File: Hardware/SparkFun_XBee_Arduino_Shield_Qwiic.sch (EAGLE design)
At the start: 68 parts, among them J4 QWIIC_RIGHT_ANGLE, U1 FSUSB30MUX_MSOP10, U2 AP63203, U3 ESD Diode, U4 FT231XS, U5 ESD Diode, U6 TXS0108, U7 TXS0108

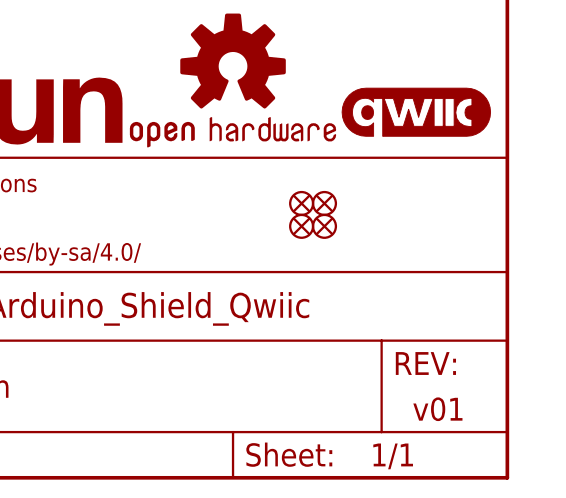
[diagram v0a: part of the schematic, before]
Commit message: Fixes wire stub DRC error
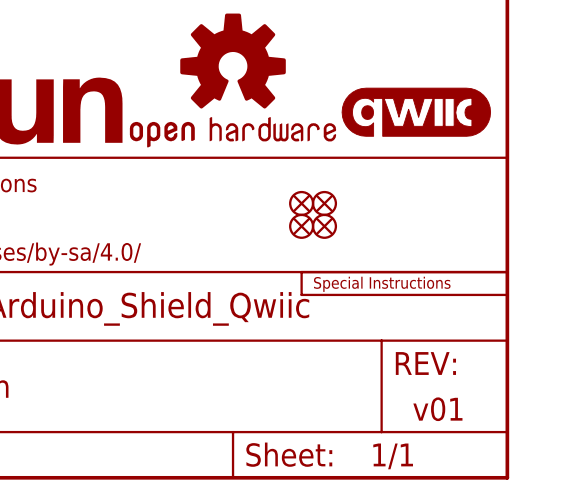
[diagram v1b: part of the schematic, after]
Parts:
- added LOGO4: SPECIAL_INSTRUCTIONS-ORDERING, SparkFun-Aesthetics:SPECIAL_INSTRUCTIONS-ORDERING
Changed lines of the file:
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@@
 <part name="SUPPLY27" library="SparkFun-PowerSymbols" deviceset="3.3V" device=""/>
 <part name="LOGO1" library="SparkFun-Aesthetics" deviceset="SFE_LOGO_NAME" device="BLANK"/>
+<part name="LOGO4" library="SparkFun-Aesthetics" deviceset="SPECIAL_INSTRUCTIONS" device="-ORDERING"/>
 </parts>
 <sheets>
@@
 </instance>
 <instance part="LOGO1" gate="G$1" x="332.74" y="33.02" smashed="yes"/>
+<instance part="LOGO4" gate="G$1" x="408.94" y="20.32" smashed="yes"/>
 </instances>
 <busses>

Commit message: Rolls to v02
* Fixes USB data lines on main UART
* Shifts ASC, RSSI nets to LEDs to be non-translated by default
* Move SCL data line to non-translated by default
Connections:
- net D+: now also U4.USBDP; no longer U4.USBDM
- net D-: now also U4.USBDM; no longer U4.USBDP
- net D1/SCL: now also J4.4, R15.1
- net D1/SCL-TRANS: no longer J4.4, R15.1
- net D10/RSSI_PWM: now also R2.1
- net D10/RSSI_PWM-TRANS: no longer R2.1
- net D5/ASSOCIATE: now also R12.1
- net D5/ASSOCIATE-TRANS: no longer R12.1
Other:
- note added: "v02"
- note removed: "v01"
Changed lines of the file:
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@@
 <text x="223.774" y="271.526" size="2.54" layer="94" font="vector" align="center">Buck Converter - AP63203</text>
 <text x="388.62" y="93.98" size="2.54" layer="94" font="vector" align="center">Qwiic - I2C</text>
-<text x="424.18" y="7.62" size="2.54" layer="94" font="vector" align="center">v01</text>
+<text x="424.18" y="7.62" size="2.54" layer="94" font="vector" align="center">v02</text>
 <text x="363.22" y="10.16" size="2.54" layer="94" font="vector" align="center">Elias Santistevan</text>
 <text x="187.96" y="71.12" size="2.54" layer="94" font="vector" align="center">Buttons and LEDs</text>
@@
 <pinref part="U6" gate="G$1" pin="A1"/>
 </segment>
+<segment>
+<pinref part="R15" gate="G$1" pin="1"/>
+<wire x1="360.68" y1="58.42" x2="363.22" y2="58.42" width="0.1524" layer="91"/>
+<label x="360.68" y="58.42" size="1.27" layer="95" font="vector" rot="R180" xref="yes"/>
+</segment>
+<segment>
+<pinref part="J4" gate="G$1" pin="4"/>
+<wire x1="406.4" y1="71.12" x2="411.48" y2="71.12" width="0.1524" layer="91"/>
+<label x="411.48" y="71.12" size="1.27" layer="95" font="vector" xref="yes"/>
+</segment>
 </net>
 <net name="GND" class="0">
@@
 <pinref part="U7" gate="G$1" pin="A2"/>
 </segment>
+<segment>
+<pinref part="R2" gate="G$1" pin="1"/>
+<label x="175.26" y="48.26" size="1.27" layer="95" font="vector" xref="yes"/>
+<wire x1="172.72" y1="45.72" x2="172.72" y2="48.26" width="0.1524" layer="91"/>
+<wire x1="172.72" y1="48.26" x2="175.26" y2="48.26" width="0.1524" layer="91"/>
+</segment>
 </net>
 <net name="D8/!DTR!" class="0">
@@
 <label x="365.76" y="132.08" size="1.27" layer="95" font="vector" rot="R180" xref="yes"/>
 <pinref part="U7" gate="G$1" pin="A4"/>
+</segment>
+<segment>
+<pinref part="R12" gate="G$1" pin="1"/>
+<label x="175.26" y="50.8" size="1.27" layer="95" font="vector" xref="yes"/>
+<wire x1="167.64" y1="45.72" x2="167.64" y2="50.8" width="0.1524" layer="91"/>
+<wire x1="167.64" y1="50.8" x2="175.26" y2="50.8" width="0.1524" layer="91"/>
 </segment>
 </net>
@@
 </segment>
 <segment>
-<label x="25.4" y="114.3" size="1.27" layer="95" font="vector" rot="R180" xref="yes"/>
-<pinref part="U4" gate="U$1" pin="USBDM"/>
-<wire x1="25.4" y1="114.3" x2="30.48" y2="114.3" width="0.1524" layer="91"/>
+<label x="25.4" y="111.76" size="1.27" layer="95" font="vector" rot="R180" xref="yes"/>
+<pinref part="U4" gate="U$1" pin="USBDP"/>
+<wire x1="25.4" y1="111.76" x2="30.48" y2="111.76" width="0.1524" layer="91"/>
 </segment>
 </net>
@@
 </segment>
 <segment>
-<label x="25.4" y="111.76" size="1.27" layer="95" font="vector" rot="R180" xref="yes"/>
-<pinref part="U4" gate="U$1" pin="USBDP"/>
-<wire x1="25.4" y1="111.76" x2="30.48" y2="111.76" width="0.1524" layer="91"/>
+<label x="25.4" y="114.3" size="1.27" layer="95" font="vector" rot="R180" xref="yes"/>
+<pinref part="U4" gate="U$1" pin="USBDM"/>
+<wire x1="25.4" y1="114.3" x2="30.48" y2="114.3" width="0.1524" layer="91"/>
 </segment>
 </net>
@@
 <pinref part="U6" gate="G$1" pin="B1"/>
 </segment>
-<segment>
-<pinref part="J4" gate="G$1" pin="4"/>
-<wire x1="406.4" y1="71.12" x2="411.48" y2="71.12" width="0.1524" layer="91"/>
-<label x="411.48" y="71.12" size="1.27" layer="95" font="vector" xref="yes"/>
-</segment>
-<segment>
-<pinref part="R15" gate="G$1" pin="1"/>
-<wire x1="360.68" y1="58.42" x2="363.22" y2="58.42" width="0.1524" layer="91"/>
-<label x="360.68" y="58.42" size="1.27" layer="95" font="vector" rot="R180" xref="yes"/>
-</segment>
 </net>
 <net name="D3/SPI_!CS!-TRANS" class="0">
@@
 <pinref part="B1" gate="G$1" pin="A2"/>
 </segment>
-<segment>
-<pinref part="R12" gate="G$1" pin="1"/>
-<label x="175.26" y="50.8" size="1.27" layer="95" font="vector" xref="yes"/>
-<wire x1="167.64" y1="45.72" x2="167.64" y2="50.8" width="0.1524" layer="91"/>
-<wire x1="167.64" y1="50.8" x2="175.26" y2="50.8" width="0.1524" layer="91"/>
-</segment>
 </net>
 <net name="D9/!SLEEP!-TRANS" class="0">
@@
 <pinref part="B1" gate="G$1" pin="A4"/>
 </segment>
-<segment>
-<pinref part="R2" gate="G$1" pin="1"/>
-<label x="175.26" y="48.26" size="1.27" layer="95" font="vector" xref="yes"/>
-<wire x1="172.72" y1="45.72" x2="172.72" y2="48.26" width="0.1524" layer="91"/>
-<wire x1="172.72" y1="48.26" x2="175.26" y2="48.26" width="0.1524" layer="91"/>
-</segment>
-</net>
+</net>

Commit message: Adds new power control circuits
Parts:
- added D6: GREEN, SparkFun-LED:LED-GREEN0603
- added IO4: JUMPER-SMT_2_NC_TRACE_SILK, SparkFun-Jumpers:JUMPER-SMT_2_NC_TRACE_SILK
- added Q1, Q2, Q3: 3.1A/30V/105mΩ, SparkFun-DiscreteSemi:MOSFET_PCH-DMG2307L
- added Q4: 5.8A/30V/35mΩ, SparkFun-DiscreteSemi:MOSFET-NCH-AO3404A
- added Q5: 20V/4.2A/52mΩ/1.4W, SparkFun-DiscreteSemi:MOSFET_PCH-DMG2305UX-7
- added Q7: (no value), SparkFun-DiscreteSemi:TRANS_PNP_DUALSOT-363
- added R10: 330, SparkFun-Resistors:330OHM-0603-1/10W-1%
- added R17: 1M, SparkFun-Resistors:1MOHM-0603-1/4W-5%
- added R18, R19, R20, R21, R22, R5, R9: 10k, SparkFun-Resistors:10KOHM-0603-1/10W-1%
- added R6: 100k, SparkFun-Resistors:100KOHM-0603-1/10W-1%
- added S4, S5: (no value), SparkFun-Switches:SWITCH-DPDT-SMD-AYZ0202
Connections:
- new net 3.3V_SW: B1.3.3V
- new net 3.3V_VREG: C2.1, C4.1, L1.2, Q5.D, Q7G1.E, U2.FB
- new net 3V3_R3: Q3.S, S5.3, S5.6
- new net N$16: R20.2, S5.1, S5.4
- new net N$17: D6.C, IO4.2
- new net N$18: Q4.D, R19.2
- new net N$19: Q7G1.B, Q7G1.C, Q7G2.B, R6.2
- new net N$20: Q5.G, Q7G2.C, R17.2
- new net N$22: Q4.G, R21.1
- new net N$24: R18.2, S4.3, S4.6
- new net N$25: Q1.G, Q1.S, Q2.G, Q2.S, R19.1
- new net N$26: R22.2, S5.2, S5.5
- new net N$27: Q3.G, R22.1
- new net N$4: D6.A, R10.2
- new net N$9: R21.2, S4.2, S4.5
- new net OE_BUS: B1.*D3, R5.2, U6.OE
- new net OE_IO: B1.D4, R9.2, U7.OE
- new net VIN_R3: B1.VIN, Q2.D, S4.1
- net 3.3V: now also Q3.D, Q5.S, Q7G2.E; no longer B1.3.3V, C2.1, C4.1, L1.2, U2.FB, U6.OE, U7.OE
- net D4/SPI_PICO: now also R10.1
- net GND: now also IO4.1, Q4.S, R17.1, R18.1, R20.1, R5.1, R6.1, R9.1
- net VIN: now also Q1.D, S4.4; no longer B1.VIN
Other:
- note added: "Power Control"
- note added: "Switches"
- moved on the sheet: ALED, C1, C10, C2, C3, C4, C5, C6, C7, C8, C9, D1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

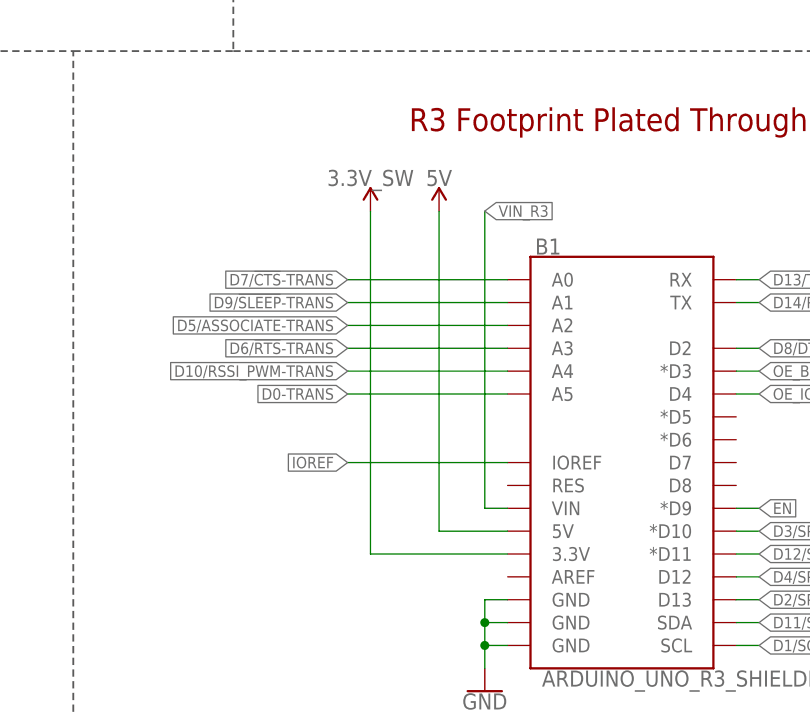
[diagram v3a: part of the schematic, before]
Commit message: Routes most of the new air wires
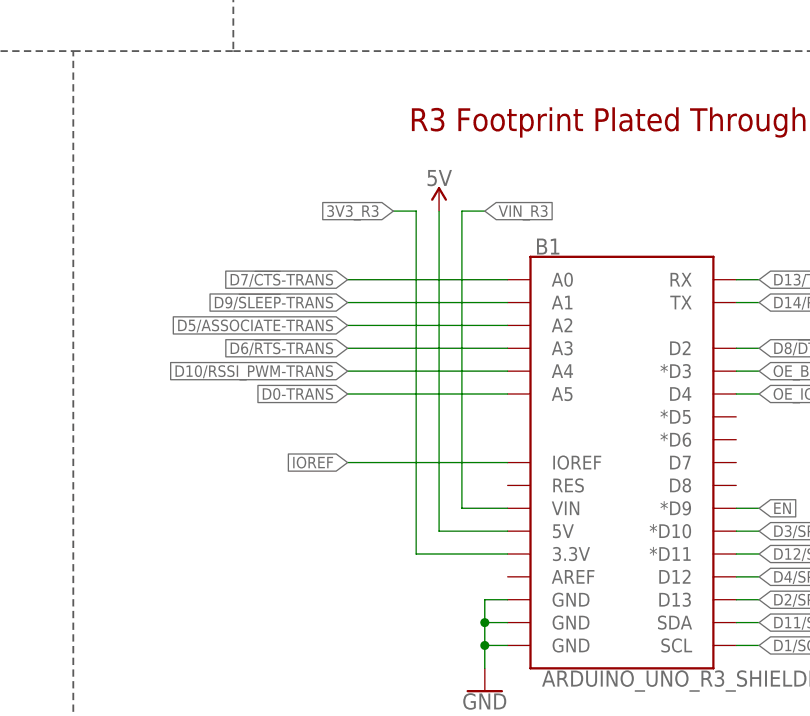
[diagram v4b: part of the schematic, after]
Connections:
- removed net 3.3V_SW: B1.3.3V
- net 3V3_R3: now also B1.3.3V
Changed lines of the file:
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@@
 <part name="GND41" library="SparkFun-PowerSymbols" deviceset="GND" device=""/>
 <part name="IO4" library="SparkFun-Jumpers" deviceset="JUMPER-SMT_2_NC_TRACE" device="_SILK" package3d_urn="urn:adsk.eagle:package:39281/1"/>
-<part name="SUPPLY28" library="SparkFun-PowerSymbols" deviceset="3.3V_SW" device=""/>
 <part name="S4" library="SparkFun-Switches" deviceset="SWITCH-DPDT" device="-SMD-AYZ0202"/>
 <part name="R18" library="SparkFun-Resistors" deviceset="10KOHM" device="-0603-1/10W-1%" value="10k"/>
@@
 <attribute name="NAME" x="187.96" y="17.272" size="1.778" layer="95" font="vector" rot="R180" align="center"/>
 </instance>
-<instance part="SUPPLY28" gate="G$1" x="129.54" y="142.24" smashed="yes">
-<attribute name="VALUE" x="129.54" y="145.034" size="1.778" layer="96" font="vector" align="bottom-center"/>
-</instance>
 <instance part="S4" gate="G$1" x="406.4" y="238.76" smashed="yes">
 <attribute name="NAME" x="406.4" y="246.634" size="1.778" layer="95" font="vector" align="bottom-center"/>
@@
 </segment>
 </net>
-<net name="3.3V_SW" class="0">
-<segment>
-<pinref part="B1" gate="G$1" pin="3.3V"/>
-<wire x1="144.78" y1="104.14" x2="129.54" y2="104.14" width="0.1524" layer="91"/>
-<wire x1="129.54" y1="104.14" x2="129.54" y2="142.24" width="0.1524" layer="91"/>
-<pinref part="SUPPLY28" gate="G$1" pin="3.3V_SW"/>
-</segment>
-</net>
 <net name="N$24" class="0">
 <segment>
@@
 <wire x1="360.68" y1="198.12" x2="350.52" y2="198.12" width="0.1524" layer="91"/>
 <label x="350.52" y="198.12" size="1.27" layer="95" font="vector" rot="MR0" xref="yes"/>
+</segment>
+<segment>
+<pinref part="B1" gate="G$1" pin="3.3V"/>
+<wire x1="144.78" y1="104.14" x2="134.62" y2="104.14" width="0.1524" layer="91"/>
+<wire x1="134.62" y1="104.14" x2="134.62" y2="142.24" width="0.1524" layer="91"/>
+<wire x1="134.62" y1="142.24" x2="132.08" y2="142.24" width="0.1524" layer="91"/>
+<label x="132.08" y="142.24" size="1.27" layer="95" font="vector" rot="R180" xref="yes"/>
 </segment>
 </net>
@@
 <segment>
 <pinref part="B1" gate="G$1" pin="VIN"/>
-<wire x1="144.78" y1="109.22" x2="142.24" y2="109.22" width="0.1524" layer="91"/>
-<wire x1="142.24" y1="109.22" x2="142.24" y2="142.24" width="0.1524" layer="91"/>
+<wire x1="144.78" y1="109.22" x2="139.7" y2="109.22" width="0.1524" layer="91"/>
+<wire x1="139.7" y1="109.22" x2="139.7" y2="142.24" width="0.1524" layer="91"/>
+<wire x1="139.7" y1="142.24" x2="142.24" y2="142.24" width="0.1524" layer="91"/>
 <label x="142.24" y="142.24" size="1.27" layer="95" font="vector" xref="yes"/>
 </segment>

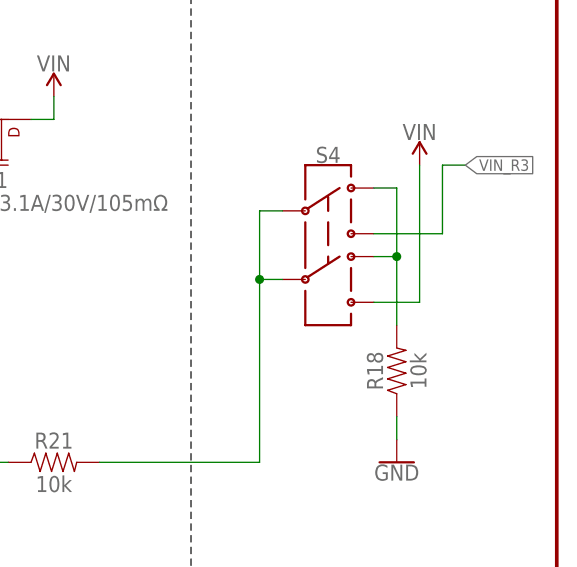
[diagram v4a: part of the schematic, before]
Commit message: Improvements to power selection
* Routes airwires
* Fixes some silk
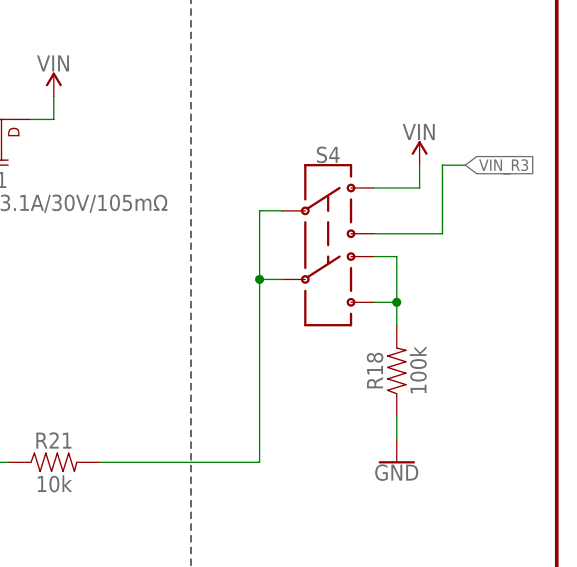
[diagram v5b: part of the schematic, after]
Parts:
- R18: value 10k -> 100k; device SparkFun-Resistors:10KOHM-0603-1/10W-1% -> SparkFun-Resistors:100KOHM-0603-1/10W-1%
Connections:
- net N$24: now also S4.4; no longer S4.3
- net VIN: now also S4.3; no longer S4.4
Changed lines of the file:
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@@
 <part name="IO4" library="SparkFun-Jumpers" deviceset="JUMPER-SMT_2_NC_TRACE" device="_SILK" package3d_urn="urn:adsk.eagle:package:39281/1"/>
 <part name="S4" library="SparkFun-Switches" deviceset="SWITCH-DPDT" device="-SMD-AYZ0202"/>
-<part name="R18" library="SparkFun-Resistors" deviceset="10KOHM" device="-0603-1/10W-1%" value="10k"/>
+<part name="R18" library="SparkFun-Resistors" deviceset="100KOHM" device="-0603-1/10W-1%" value="100k"/>
 <part name="GND42" library="SparkFun-PowerSymbols" deviceset="GND" device=""/>
 <part name="SUPPLY34" library="SparkFun-PowerSymbols" deviceset="VIN" device=""/>
@@
 </segment>
 <segment>
-<pinref part="S4" gate="G$1" pin="4"/>
-<wire x1="411.48" y1="231.14" x2="416.56" y2="231.14" width="0.1524" layer="91"/>
-<wire x1="416.56" y1="231.14" x2="416.56" y2="246.38" width="0.1524" layer="91"/>
 <pinref part="SUPPLY34" gate="G$1" pin="VIN"/>
+<pinref part="S4" gate="G$1" pin="3"/>
+<wire x1="416.56" y1="243.84" x2="416.56" y2="246.38" width="0.1524" layer="91"/>
+<wire x1="411.48" y1="243.84" x2="416.56" y2="243.84" width="0.1524" layer="91"/>
 </segment>
 <segment>
@@
 <net name="N$24" class="0">
 <segment>
-<pinref part="S4" gate="G$1" pin="3"/>
-<wire x1="411.48" y1="243.84" x2="414.02" y2="243.84" width="0.1524" layer="91"/>
-<wire x1="414.02" y1="243.84" x2="414.02" y2="236.22" width="0.1524" layer="91"/>
 <pinref part="S4" gate="G$1" pin="6"/>
-<wire x1="414.02" y1="236.22" x2="414.02" y2="228.6" width="0.1524" layer="91"/>
+<wire x1="414.02" y1="236.22" x2="414.02" y2="231.14" width="0.1524" layer="91"/>
+<wire x1="414.02" y1="231.14" x2="414.02" y2="228.6" width="0.1524" layer="91"/>
 <wire x1="411.48" y1="236.22" x2="414.02" y2="236.22" width="0.1524" layer="91"/>
-<junction x="414.02" y="236.22"/>
 <pinref part="R18" gate="G$1" pin="2"/>
-</segment>
-</net>
+<pinref part="S4" gate="G$1" pin="4"/>
+<wire x1="411.48" y1="231.14" x2="414.02" y2="231.14" width="0.1524" layer="91"/>
+<junction x="414.02" y="231.14"/>
+</segment>
+</net>

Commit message: Adds silk
* Adds enable net, needs route
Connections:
- net N$16 renamed OFF_3V3
- net N$24 renamed OFF_VIN
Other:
- moved on the sheet: C1, C2, C3, C4, C6, D1, D5, DIRECT_USB, J2, L1, Q5, Q7G1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

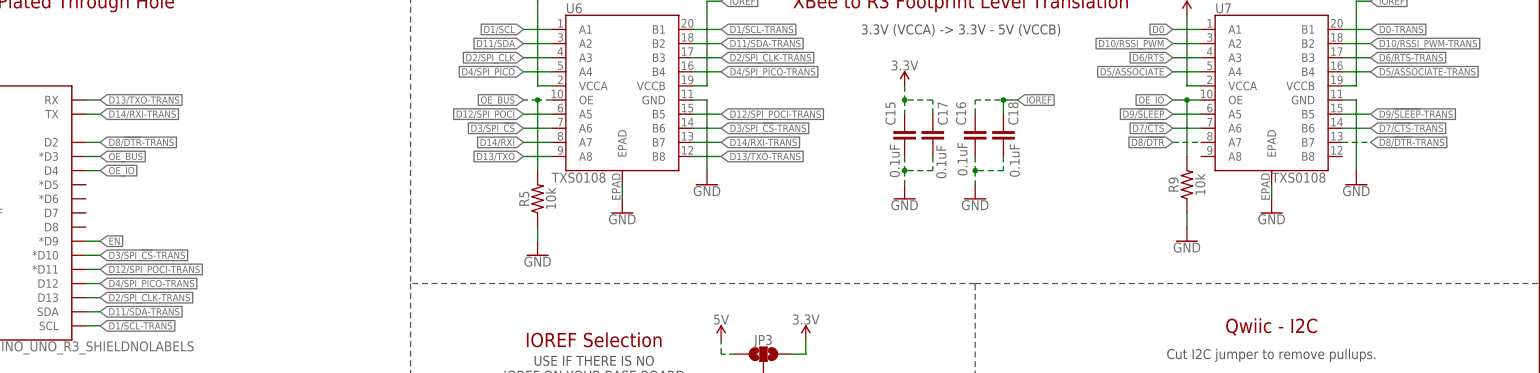
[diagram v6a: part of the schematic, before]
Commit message: Routes enable pin
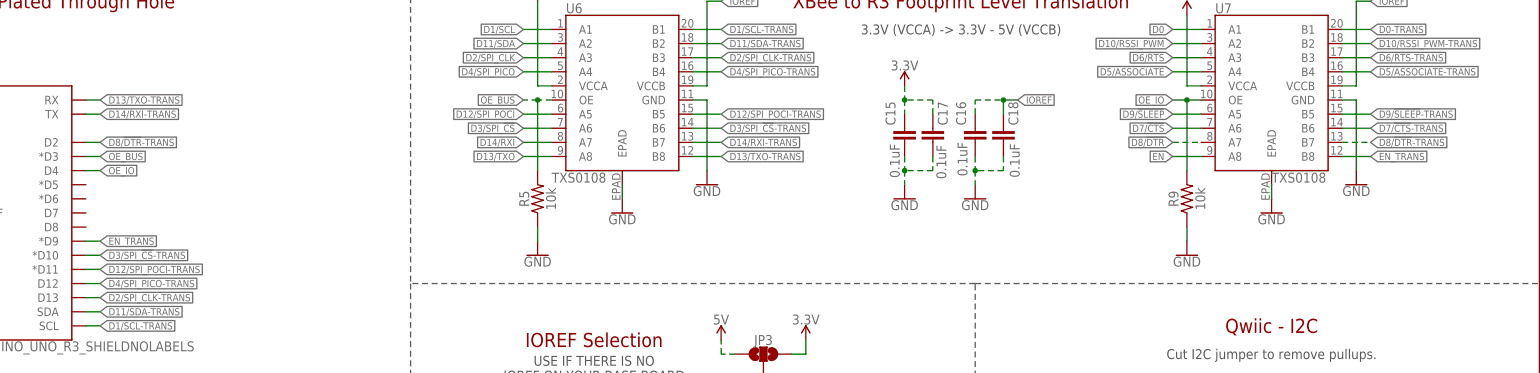
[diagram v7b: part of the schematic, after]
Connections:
- new net EN_TRANS: B1.*D9, U7.B8
- net EN: now also U7.A8; no longer B1.*D9
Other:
- moved on the sheet: R9
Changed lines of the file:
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@@
 <attribute name="VALUE" x="251.46" y="106.426" size="1.778" layer="96" font="vector" rot="MR0" align="top-center"/>
 </instance>
-<instance part="R9" gate="G$1" x="368.3" y="119.38" smashed="yes" rot="R90">
-<attribute name="NAME" x="366.776" y="119.38" size="1.778" layer="95" font="vector" rot="R90" align="bottom-center"/>
-<attribute name="VALUE" x="369.824" y="119.38" size="1.778" layer="96" font="vector" rot="R90" align="top-center"/>
-</instance>
-<instance part="GND38" gate="1" x="368.3" y="109.22" smashed="yes" rot="MR0">
-<attribute name="VALUE" x="368.3" y="108.966" size="1.778" layer="96" font="vector" rot="MR0" align="top-center"/>
+<instance part="R9" gate="G$1" x="368.3" y="116.84" smashed="yes" rot="R90">
+<attribute name="NAME" x="366.776" y="116.84" size="1.778" layer="95" font="vector" rot="R90" align="bottom-center"/>
+<attribute name="VALUE" x="369.824" y="116.84" size="1.778" layer="96" font="vector" rot="R90" align="top-center"/>
+</instance>
+<instance part="GND38" gate="1" x="368.3" y="106.68" smashed="yes" rot="MR0">
+<attribute name="VALUE" x="368.3" y="106.426" size="1.778" layer="96" font="vector" rot="MR0" align="top-center"/>
 </instance>
 <instance part="D6" gate="G$1" x="182.88" y="30.48" smashed="yes">
@@
 <pinref part="R9" gate="G$1" pin="1"/>
 <pinref part="GND38" gate="1" pin="GND"/>
-<wire x1="368.3" y1="111.76" x2="368.3" y2="114.3" width="0.1524" layer="91"/>
+<wire x1="368.3" y1="109.22" x2="368.3" y2="111.76" width="0.1524" layer="91"/>
 </segment>
 <segment>
@@
 </segment>
 <segment>
-<wire x1="172.72" y1="109.22" x2="170.18" y2="109.22" width="0.1524" layer="91"/>
-<label x="172.72" y="109.22" size="1.27" layer="95" font="vector" xref="yes"/>
-<pinref part="B1" gate="G$1" pin="*D9"/>
+<pinref part="U7" gate="G$1" pin="A8"/>
+<wire x1="365.76" y1="124.46" x2="370.84" y2="124.46" width="0.1524" layer="91"/>
+<label x="365.76" y="124.46" size="1.27" layer="95" font="vector" rot="R180" xref="yes"/>
 </segment>
 </net>
@@
 <pinref part="R9" gate="G$1" pin="2"/>
 <wire x1="368.3" y1="134.62" x2="370.84" y2="134.62" width="0.1524" layer="91"/>
-<wire x1="368.3" y1="124.46" x2="368.3" y2="134.62" width="0.1524" layer="91"/>
+<wire x1="368.3" y1="121.92" x2="368.3" y2="134.62" width="0.1524" layer="91"/>
 <junction x="368.3" y="134.62"/>
 </segment>
@@
 </segment>
 </net>
+<net name="EN_TRANS" class="0">
+<segment>
+<pinref part="U7" gate="G$1" pin="B8"/>
+<wire x1="396.24" y1="124.46" x2="401.32" y2="124.46" width="0.1524" layer="91"/>
+<label x="401.32" y="124.46" size="1.27" layer="95" font="vector" xref="yes"/>
+</segment>
+<segment>
+<pinref part="B1" gate="G$1" pin="*D9"/>
+<wire x1="172.72" y1="109.22" x2="170.18" y2="109.22" width="0.1524" layer="91"/>
+<label x="172.72" y="109.22" size="1.27" layer="95" font="vector" xref="yes"/>
+</segment>
+</net>
